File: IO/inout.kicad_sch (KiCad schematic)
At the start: 11 parts, among them J7 AudioJack2_SwitchT, J8 AudioJack2_SwitchT

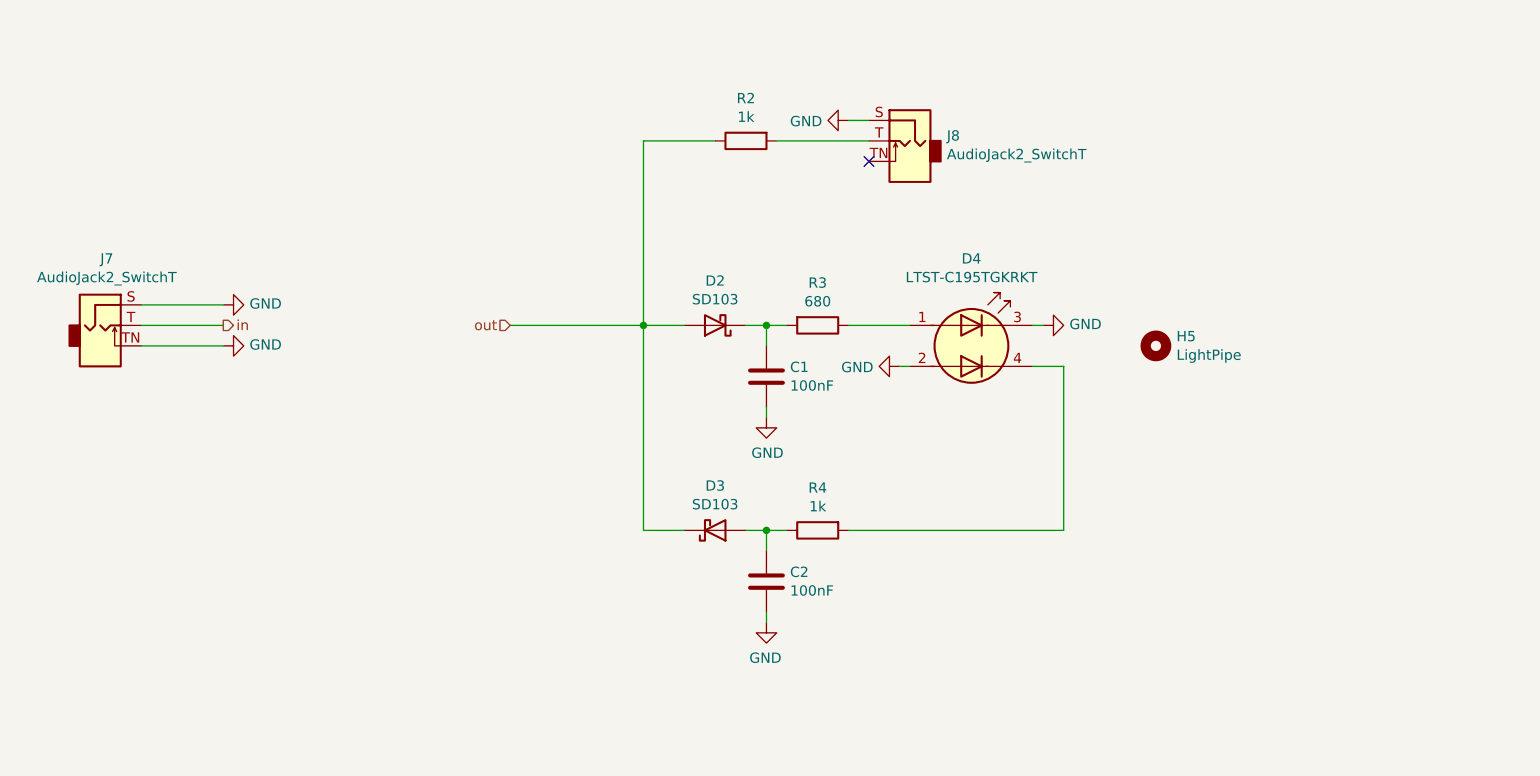
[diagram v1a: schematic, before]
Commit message: Reduce output capacitive load
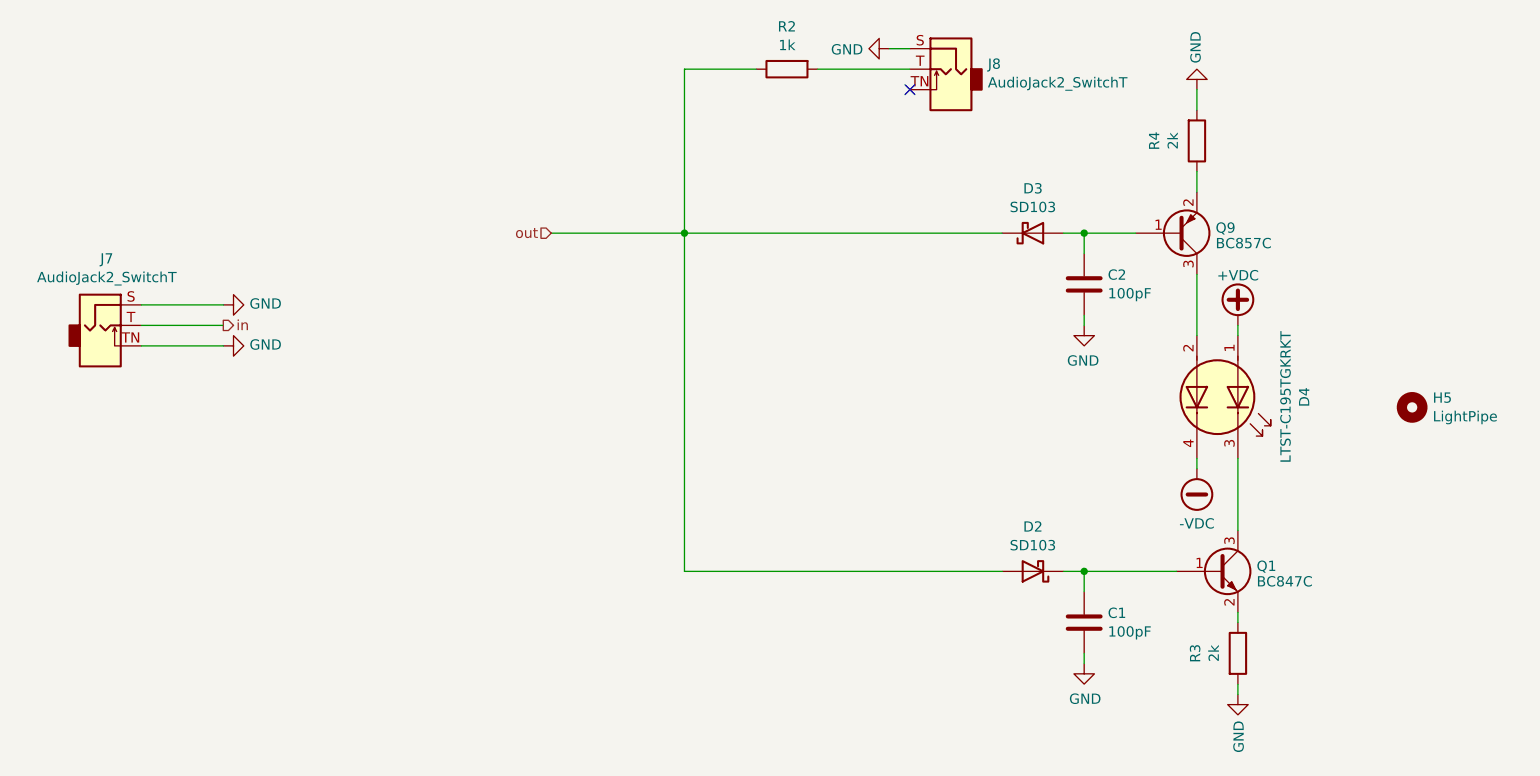
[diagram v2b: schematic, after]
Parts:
- added Q1: BC847C, Package_TO_SOT_SMD:SOT-23, symbol Transistor_BJT:BC847
- added Q9: BC857C, Package_TO_SOT_SMD:SOT-23, symbol Transistor_BJT:BC857
- C1, C2: value 100nF -> 100pF
- R3: value 680 -> 2k
- R4: value 1k -> 2k
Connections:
- net GND: now also R3.2, R4.2; no longer D4.2 (A2), D4.3 (K1)
- net at R3.1: now also Q1.2 (E); no longer D4.1 (A1)
- net -VDC: now reaches D4.4 (K2)
- net -VDC: no longer R4.2
- net at C1.1, D2.1 (K): now also Q1.1 (B); no longer R3.2
- net at C2.1, D3.2 (A): now also Q9.1 (B); no longer R4.1
- new net: D4.2 (A2), Q9.3 (C)
- new net: D4.3 (K1), Q1.3 (C)
- new net: Q9.2 (E), R4.1
- new net +VDC: D4.1 (A1)
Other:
- moved on the sheet: C1, C2, D2, D3, D4, H5, J8, R2, R3, R4

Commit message: Update sheet metadata
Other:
- company: (none) -> GuavTek
- title: (none) -> M2IDI_IO
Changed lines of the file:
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@@
 (kicad_sch (version 20230121) (generator eeschema)
   (paper "A4")
+  (title_block
+    (title "M2IDI_IO")
+    (date "2023-04-19")
+    (rev "1.1")
+    (company "GuavTek")
+  )
   (junction (at 198.12 97.79) (diameter 0) (color 0 0 0 0)
   )

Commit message: Fix metadata
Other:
- title: M2IDI_IO -> M2IDI - TANGLE IO
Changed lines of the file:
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@@
   (paper "A4")
   (title_block
-    (title "M2IDI_IO")
+    (title "M2IDI - TANGLE IO")
     (date "2023-04-19")
     (rev "1.1")
